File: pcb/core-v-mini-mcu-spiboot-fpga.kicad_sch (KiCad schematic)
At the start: 36 parts, among them J1 Conn_02x10_Odd_Even, P1 USB Micro, U1 93C46B, U2 FT4232H, U3 W25Q

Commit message: Revision 2: Converted to the available 56 pin QFN package, added missing oscillator
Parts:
- removed U2: FT4232H, Package_QFP:LQFP-64_10x10mm_P0.5mm, symbol Interface_USB:FT4232H
- added R13: 10k, Resistor_SMD:R_0603_1608Metric, symbol Device:R_Small
- added U2: FT4232H-56Q, Package_DFN_QFN:QFN-56-1EP_8x8mm_P0.5mm_EP5.9x5.9mm, symbol core-v-mini-mcu-spiboot-fpga-lib:FT4232H-56Q
- added U4: SIT2001BI-S2-33E-12.000000D, Package_TO_SOT_SMD:TSOT-23-5_HandSoldering, symbol pkl_device:pkl_oscillator_sit2001
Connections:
- net +3V3: now also C1.2, R13.2, U2.16 (VCCIO), U2.36 (VCCIO), U2.44 (VREGIN), U2.50 (VCCIO), U4.4 (VDD)
- net A4: now also U2.17 (ADBUS4)
- net A5: now also U2.18 (ADBUS5)
- net A6: now also U2.19 (ADBUS6)
- net A7: now also U2.20 (ADBUS7)
- net B5: now also U2.27 (BDBUS5)
- net C2: now also U2.34 (CDBUS2)
- net C3: now also U2.35 (CDBUS3)
- net C4: now also U2.37 (CDBUS4)
- net C5: now also U2.38 (CDBUS5)
- net C6: now also U2.39 (CDBUS6)
- net C7: now also U2.40 (CDBUS7)
- net CK12MHZ: now also U2.3 (OSCI), U4.5 (OUT)
- net D2: now also U2.47 (DDBUS2)
- net D3: now also U2.48 (DDBUS3)
- net D4: now also U2.49 (DDBUS4)
- net D5: now also U2.51 (DDBUS5)
- net D6: now also U2.52 (DDBUS6)
- net D7: now also U2.53 (DDBUS7)
- net EECS: now also U2.1 (EECS)
- net FLASH_MISO: now also U2.24 (BDBUS2)
- net FLASH_MOSI: now also U2.23 (BDBUS1)
- net FLASH_SCK: now also U2.22 (BDBUS0)
- net GND: now also C1.1, U2.10 (TEST), U2.21 (GND), U2.41 (GND), U2.45 (GND), U2.57 (GND), U4.1 (GND); no longer C1.2
- net RX0: now also U2.33 (CDBUS1)
- net RX1: now also U2.46 (DDBUS1)
- net SPI_CS: now also U2.25 (BDBUS3)
- net TCK: now also U2.12 (ADBUS0)
- net TDI: now also U2.13 (ADBUS1)
- net TDO: now also U2.14 (ADBUS2)
- net TMS: now also U2.15 (ADBUS3)
- net TX0: now also U2.32 (CDBUS0)
- net TX1: now also U2.42 (DDBUS0)
- net VCORE: now also U2.2 (VCORE), U2.31 (VCORE), U2.43 (VREGOUT); no longer C1.1
- net iCE_CDONE: now also U2.28 (BDBUS6)
- net iCE_SS_B: now also U2.26 (BDBUS4)
- net at C8.1, C9.1, L2.2: now also U2.9 (VPLL)
- net at C6.1, C7.1, L1.2: now also U2.5 (VPHY)
- net at R7.1: now also U2.11 (~{RESET})
- net at R8.1: now also U2.29 (BDBUS7)
- net at R6.2: now also U2.6 (REF)
- net at R4.1, U1.3 (DI): now also U2.55 (EEDATA)
- net at R3.1, U1.2 (SCLK): now also U2.56 (EECLK)
- net USBDM renamed USB_D-
- net USB_D-: now also U2.7 (DM)
- net USBDP renamed USB_D+
- net USB_D+: now also U2.8 (DP)
- new net: R13.1, U4.3 (OE/~{ST}/NC)
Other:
- note added: "MEMS oscillator, keep away from helium ;-)"
- note added: "SPI FLASH"
- note removed: "SPI FPGA"

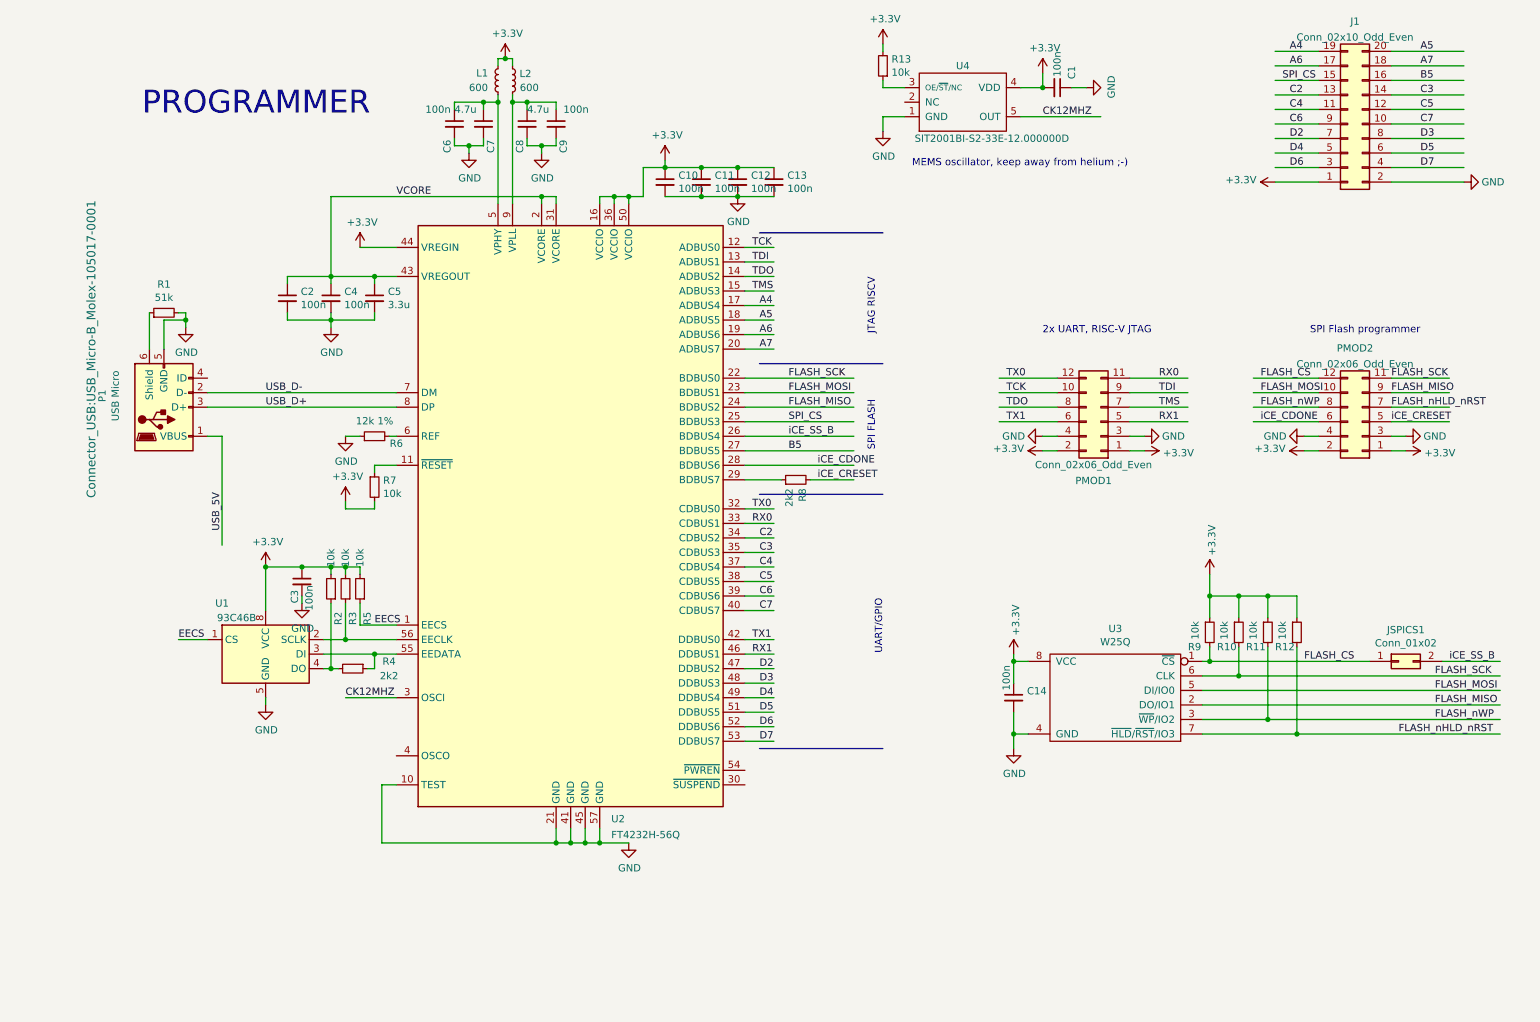
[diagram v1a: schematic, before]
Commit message: QFN version
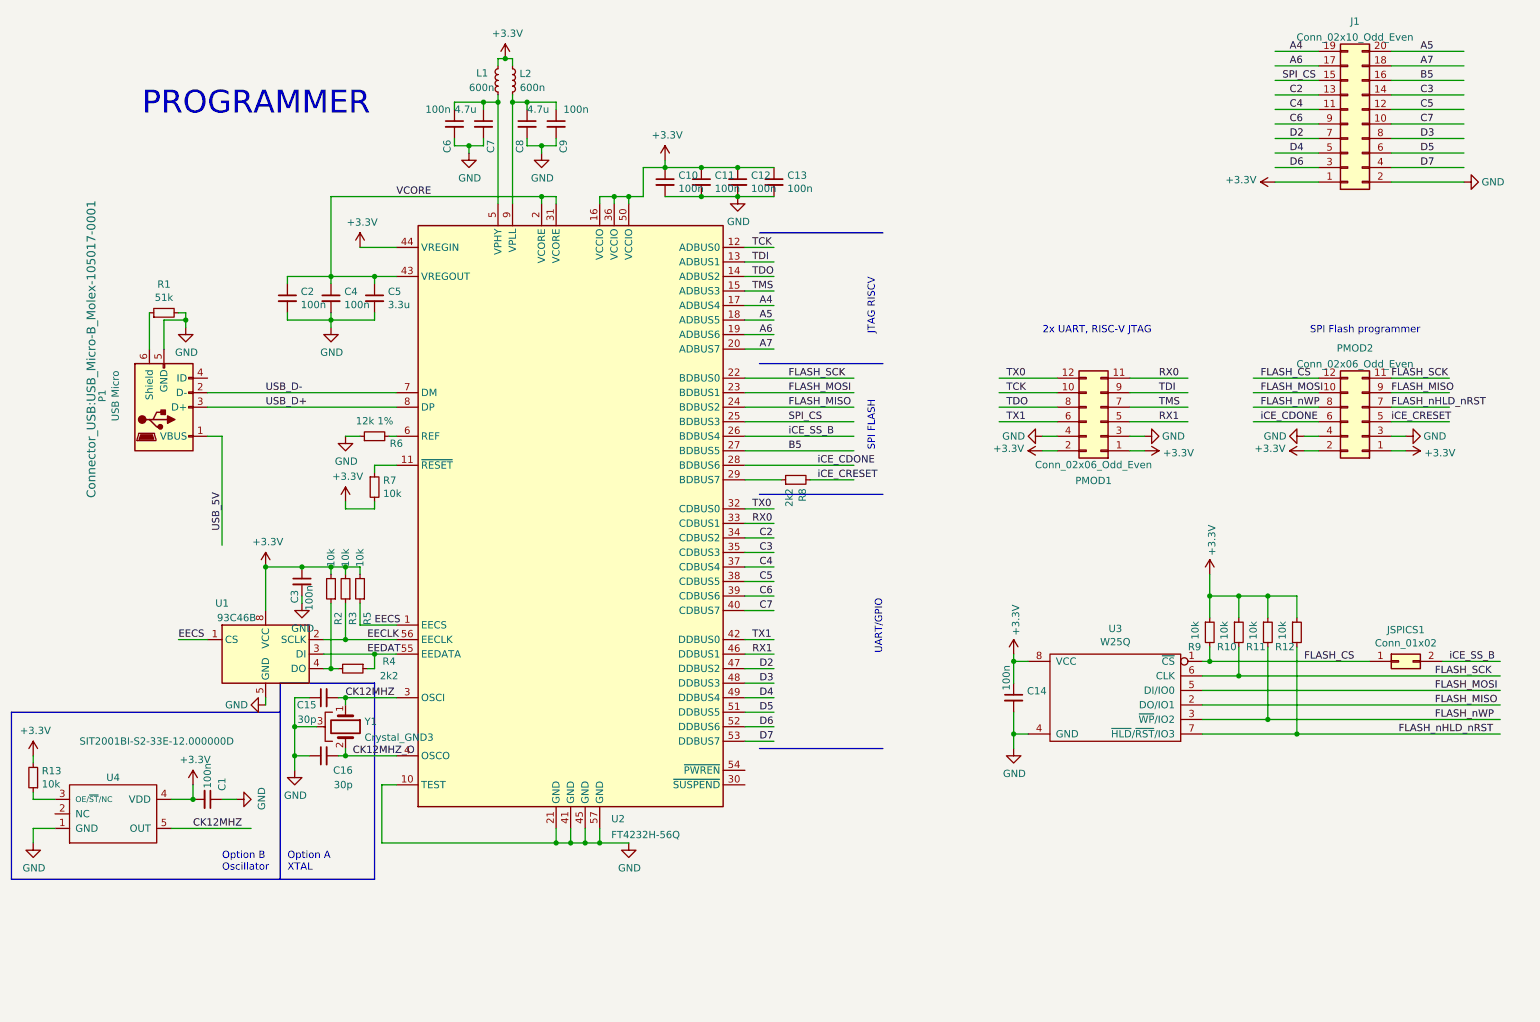
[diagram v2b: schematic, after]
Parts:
- added C15, C16: 30p, Capacitor_SMD:C_0603_1608Metric, symbol Device:C_Small
- added Y1: Crystal_GND3, Crystal:Crystal_DS15_D1.5mm_L5.0mm_Horizontal_1EP_style1, symbol Device:Crystal_GND3
- L1, L2: value 600 -> 600n
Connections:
- net CK12MHZ: now also C15.2, Y1.1
- net GND: now also C15.1, C16.1, Y1.3
- net EECLK: now reaches R3.1, U1.2 (SCLK), U2.56 (EECLK)
- net CK12MHZ_O: now reaches U2.4 (OSCO)
- net CK12MHZ_O: now also C16.2, Y1.2
- net EEDAT: now reaches R4.1, U1.3 (DI), U2.55 (EEDATA)
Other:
- note added: "Option A XTAL"
- note added: "Option B Oscillator"
- note removed: "MEMS oscillator, keep away from helium ;-)"
- moved on the sheet: C1, R13, U4

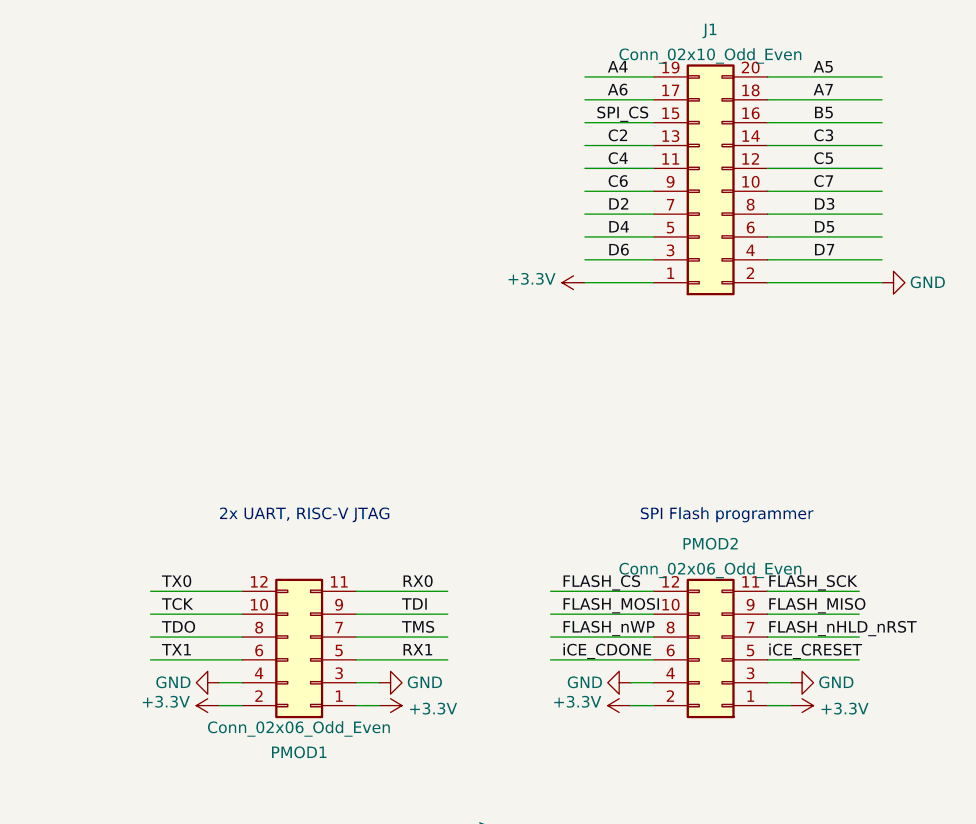
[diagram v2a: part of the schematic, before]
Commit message: QFN version
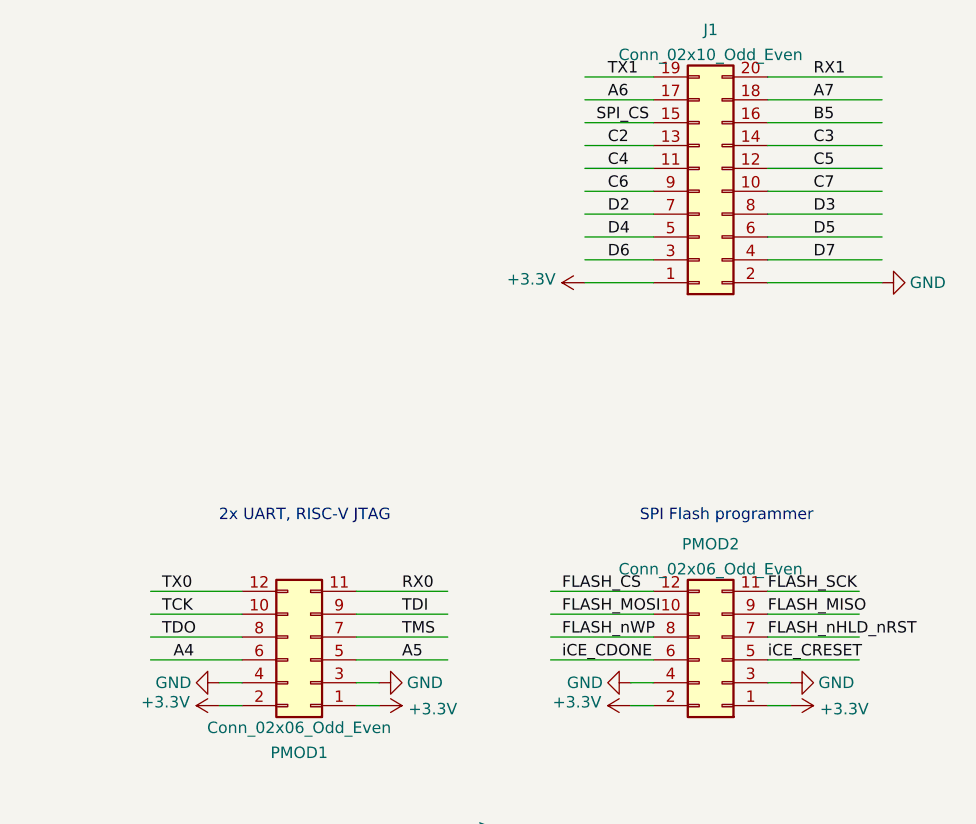
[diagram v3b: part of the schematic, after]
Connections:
- net A4: now also PMOD1.6 (Pin_6); no longer J1.19 (Pin_19)
- net A5: now also PMOD1.5 (Pin_5); no longer J1.20 (Pin_20)
- net RX1: now also J1.20 (Pin_20); no longer PMOD1.5 (Pin_5)
- net TX1: now also J1.19 (Pin_19); no longer PMOD1.6 (Pin_6)
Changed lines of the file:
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@@
-    (effects (font (size 1.27 1.27)) (justify left bottom))
-  )
-  (label "RX1" (at 213.36 92.71 0)
     (effects (font (size 1.27 1.27)) (justify left bottom))
   )
@@
     (effects (font (size 1.27 1.27)) (justify left bottom))
   )
-  (label "TX1" (at 186.69 92.71 0)
+  (label "TX1" (at 236.22 27.94 0)
     (effects (font (size 1.27 1.27)) (justify left bottom))
   )
@@
     (effects (font (size 1.27 1.27)) (justify left bottom))
   )
+  (label "RX1" (at 142.24 133.35 0)
+    (effects (font (size 1.27 1.27)) (justify left bottom))
+  )
   (label "FLASH_nHLD_nRST" (at 255.27 147.32 0)
     (effects (font (size 1.27 1.27)) (justify left bottom))
@@
     (effects (font (size 1.27 1.27)) (justify left bottom))
   )
-  (label "A5" (at 259.08 27.94 0)
+  (label "A5" (at 213.36 92.71 0)
     (effects (font (size 1.27 1.27)) (justify left bottom))
   )
@@
     (effects (font (size 1.27 1.27)) (justify left bottom))
   )
-  (label "RX1" (at 142.24 133.35 0)
+  (label "RX1" (at 259.08 27.94 0)
     (effects (font (size 1.27 1.27)) (justify left bottom))
   )
@@
     (effects (font (size 1.27 1.27)) (justify left bottom))
   )
-  (label "A4" (at 236.22 27.94 0)
-    (effects (font (size 1.27 1.27)) (justify left bottom))
-  )
+  (label "A4" (at 187.96 92.71 0)
+    (effects (font (size 1.27 1.27)) (justify left bottom))
+  )
